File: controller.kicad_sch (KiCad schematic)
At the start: 43 parts, among them J10 Btn 3, J11 GND, J3 JTAG, J4 DM3AT-SF-PEJM5, J5 Volume, J6 Btn 0, J7 RS485, J8 Btn 1, J9 Btn 2, SW1 Reset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

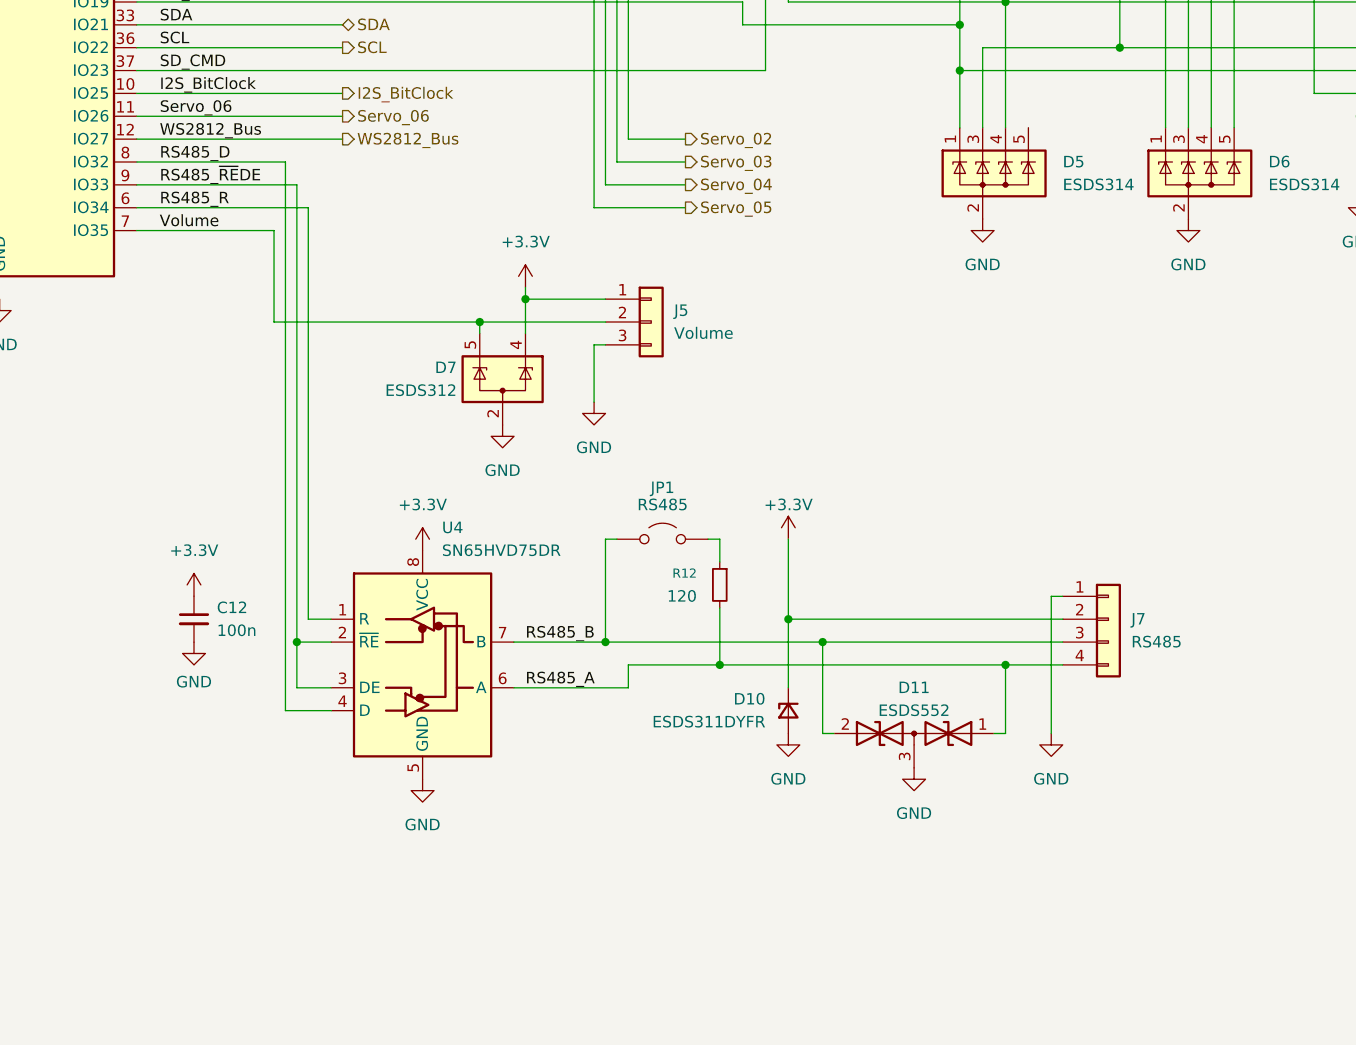
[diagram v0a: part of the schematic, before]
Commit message: Changed the WS2812 driver IC Optimized the Analog GND and AVCC routing Changed RS485 driver Removed TVS Diode at the RS485 driver (already has 15kV rating)
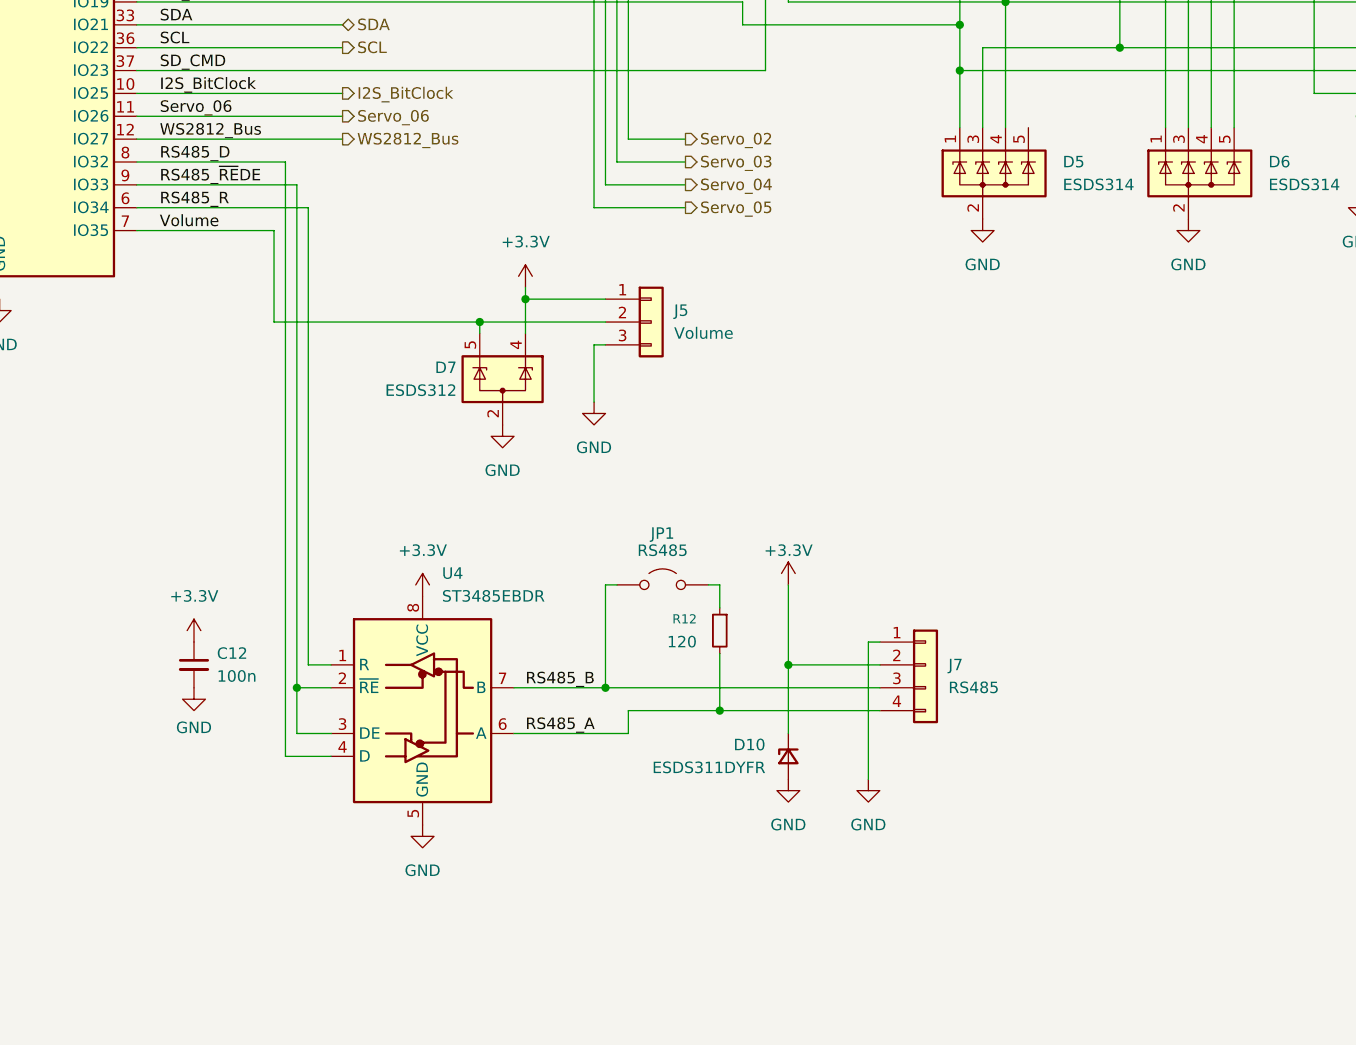
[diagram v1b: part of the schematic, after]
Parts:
- removed D11: ESDS552, Package_TO_SOT_SMD:SOT-23-3, symbol Device:D_TVS_Dual_AAC
- U4: value SN65HVD75DR -> ST3485EBDR
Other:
- moved on the sheet: C12, J7, JP1, R12, U4

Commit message: Footprint changes
Changed WS2812 from 5050 to 2020
Changed ESP32 to correct revision
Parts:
- U3: footprint RF_Module:ESP32-WROOM-32D -> RF_Module:ESP32-WROOM-32E
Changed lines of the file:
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@@
 			)
 		)
-		(property "Footprint" "RF_Module:ESP32-WROOM-32D"
+		(property "Footprint" "RF_Module:ESP32-WROOM-32E"
 			(at 92.71 105.41 0)
 			(effects

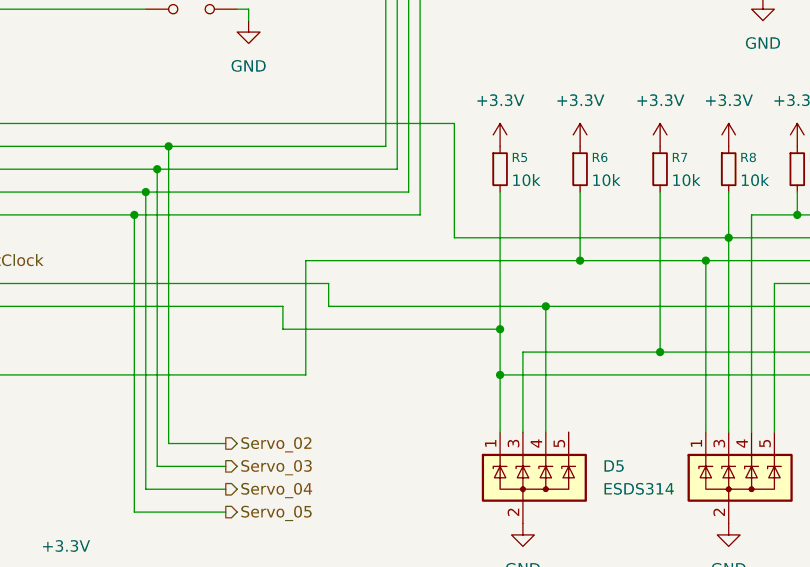
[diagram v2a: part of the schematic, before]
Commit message: Silkscreen fix
Fixed wrong silkcreen text for the DAC Voltage-Source. USB and +5V are flipped
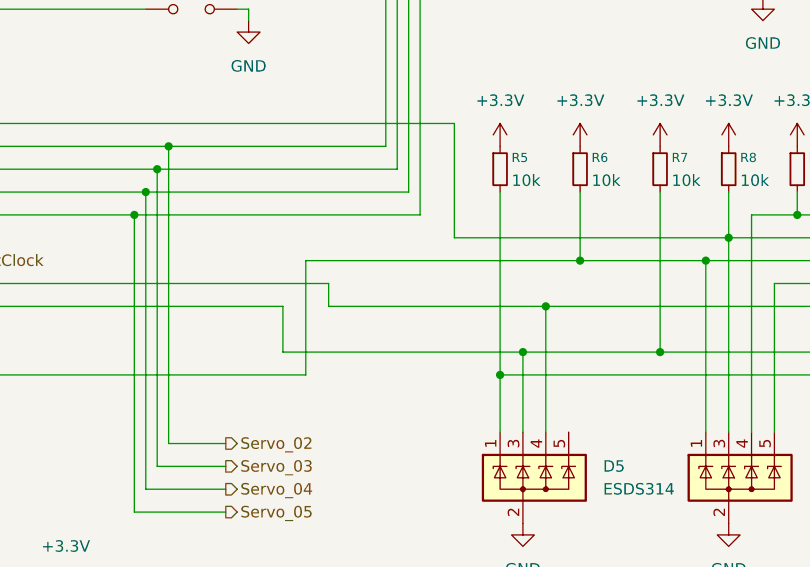
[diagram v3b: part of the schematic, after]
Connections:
- net SD_DAT0: now also D5.3 (K), J4.7 (DAT0), R7.2; no longer D5.1 (K), J4.8 (DAT1), R5.2
- new net: D5.1 (K), J4.8 (DAT1), R5.2
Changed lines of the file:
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@@
-	)
-	(junction
-		(at 182.88 76.2)
-		(diameter 0)
-		(color 0 0 0 0)
 	)
 	(junction
@@
 	)
 	(junction
+		(at 185.42 78.74)
+		(diameter 0)
+		(color 0 0 0 0)
+	)
+	(junction
 		(at 33.02 127)
 		(diameter 0)
@@
 	(wire
 		(pts
-			(xy 158.75 76.2) (xy 182.88 76.2)
-		)
-		(stroke
-			(width 0)
-			(type default)
-		)
-	)
-	(wire
-		(pts
 			(xy 33.02 157.48) (xy 33.02 154.94)
 		)
@@
 	(wire
 		(pts
-			(xy 182.88 60.96) (xy 182.88 76.2)
+			(xy 182.88 60.96) (xy 182.88 81.28)
 		)
 		(stroke
@@
 	(wire
 		(pts
-			(xy 182.88 76.2) (xy 182.88 81.28)
+			(xy 158.75 78.74) (xy 185.42 78.74)
 		)
 		(stroke
@@
 	(wire
 		(pts
+			(xy 158.75 73.66) (xy 158.75 78.74)
+		)
+		(stroke
+			(width 0)
+			(type default)
+		)
+	)
+	(wire
+		(pts
 			(xy 191.77 68.58) (xy 205.74 68.58)
 		)
@@
 		)
 		(stroke
-			(width 0)
-			(type default)
-		)
-	)
-	(wire
-		(pts
-			(xy 158.75 73.66) (xy 158.75 76.2)
-		)
-		(stroke
